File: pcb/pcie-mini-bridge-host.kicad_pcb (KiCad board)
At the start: 4 copper layers, 66.2 x 14 mm, 15 parts, among them J1 PCIe_x1, J2 USB_C_Receptacle, U1 TPS25944L, U2 TPS25944L

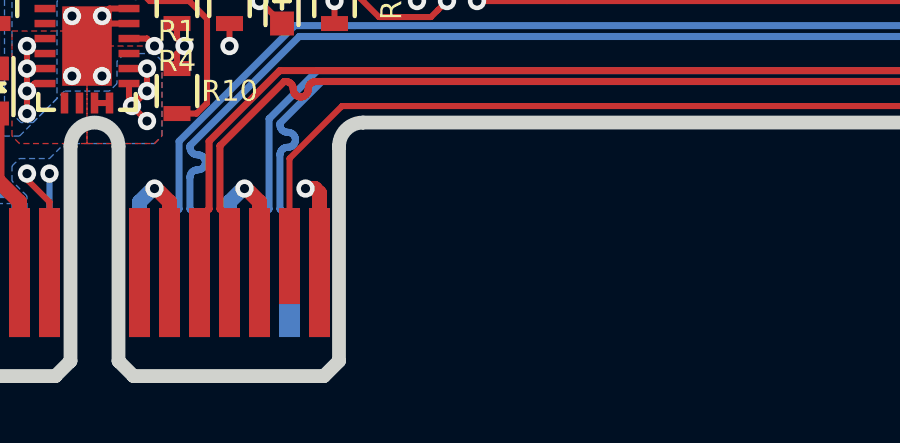
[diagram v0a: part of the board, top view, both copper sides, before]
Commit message: dev pcb layout, outline and hole parts
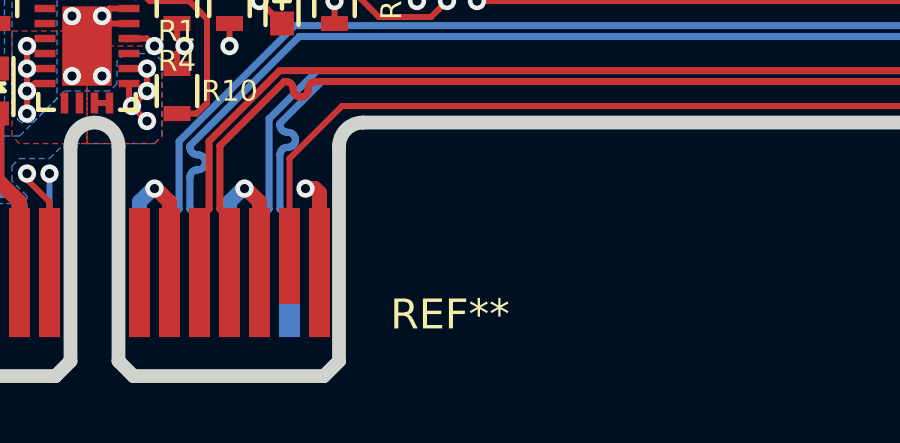
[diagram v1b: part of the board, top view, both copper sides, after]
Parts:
- added REF**: PCIe_CardOutline_x1_LPHL, pcie-mini-bridge-special:PCIe_CardOutline_x1_LPHL, F.Cu at (170.0, 90.0)

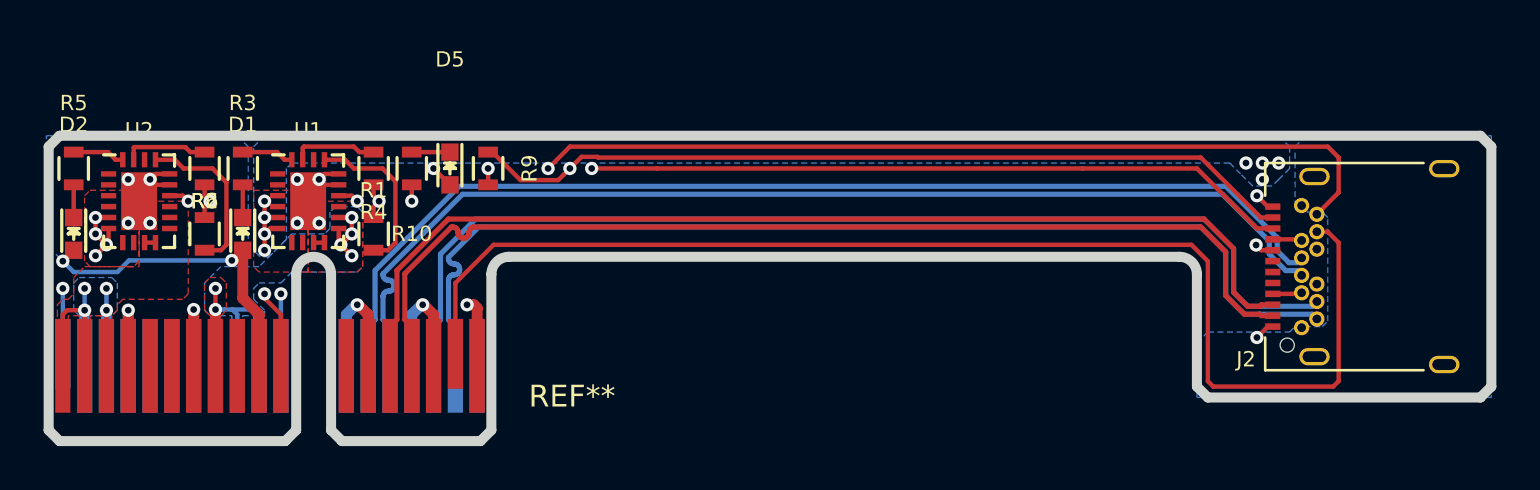
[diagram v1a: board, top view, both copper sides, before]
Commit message: fix drc and dfm problems and make rev 1 gerbers
* fix usb c recp. drc. change suggested .7/.4mm th/drills to .6728/.368mm th/drills to meet 6mil annular rings and 5mil spacing. remove slots.
* clean up silk, add board labels
* fix soldermask sizing to .051mm clearance with .077mm min width
* remove PCIe length matching on host board because host + dev is correct length
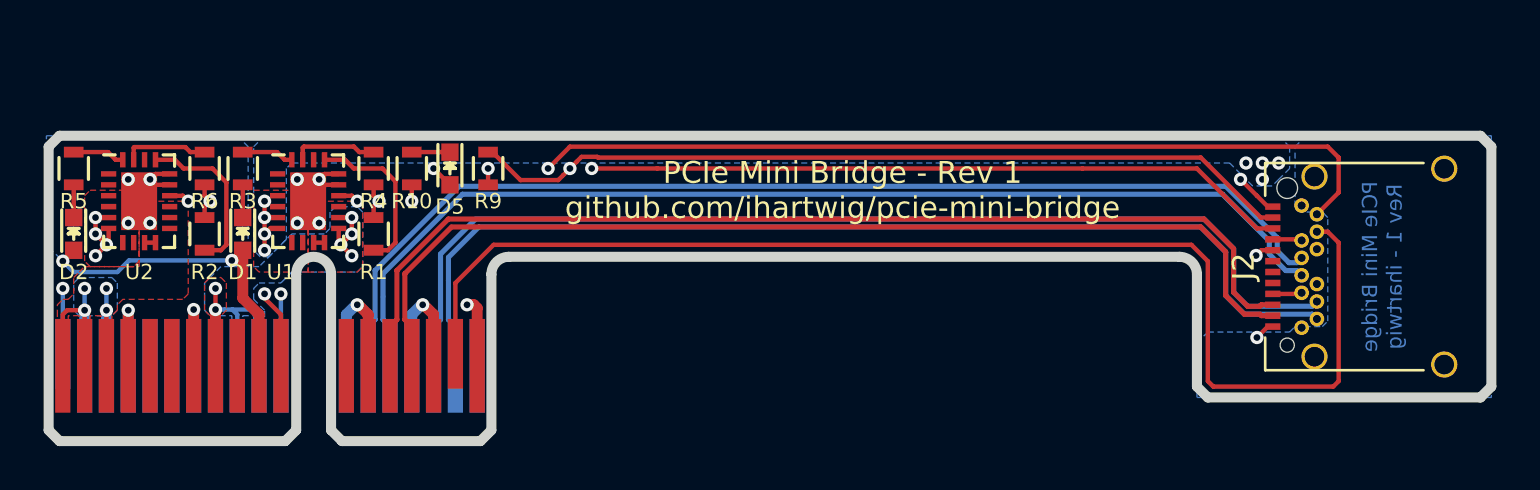
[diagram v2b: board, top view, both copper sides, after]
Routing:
- net GND: track 36.0 -> 37.0 mm
- net /PE_R0-: track 49.0 -> 48.4 mm
- net /PE_T0-: track 48.5 -> 47.9 mm
- net /PE_REFCLK-: track 50.5 -> 49.9 mm
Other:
- rule solder_mask_min_width: 0.711 -> 0.077
- board text added: "PCIe Mini Bridge - Rev 1 github.com/ihartwig/pcie-mini-bridge"
- board text added: "PCIe Mini Bridge Rev 1 - ihartwig"
